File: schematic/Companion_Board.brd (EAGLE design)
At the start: 97 x 52 mm, 51 parts, among them J10 QSH-030-01-X-D-A, Q1 16MHz

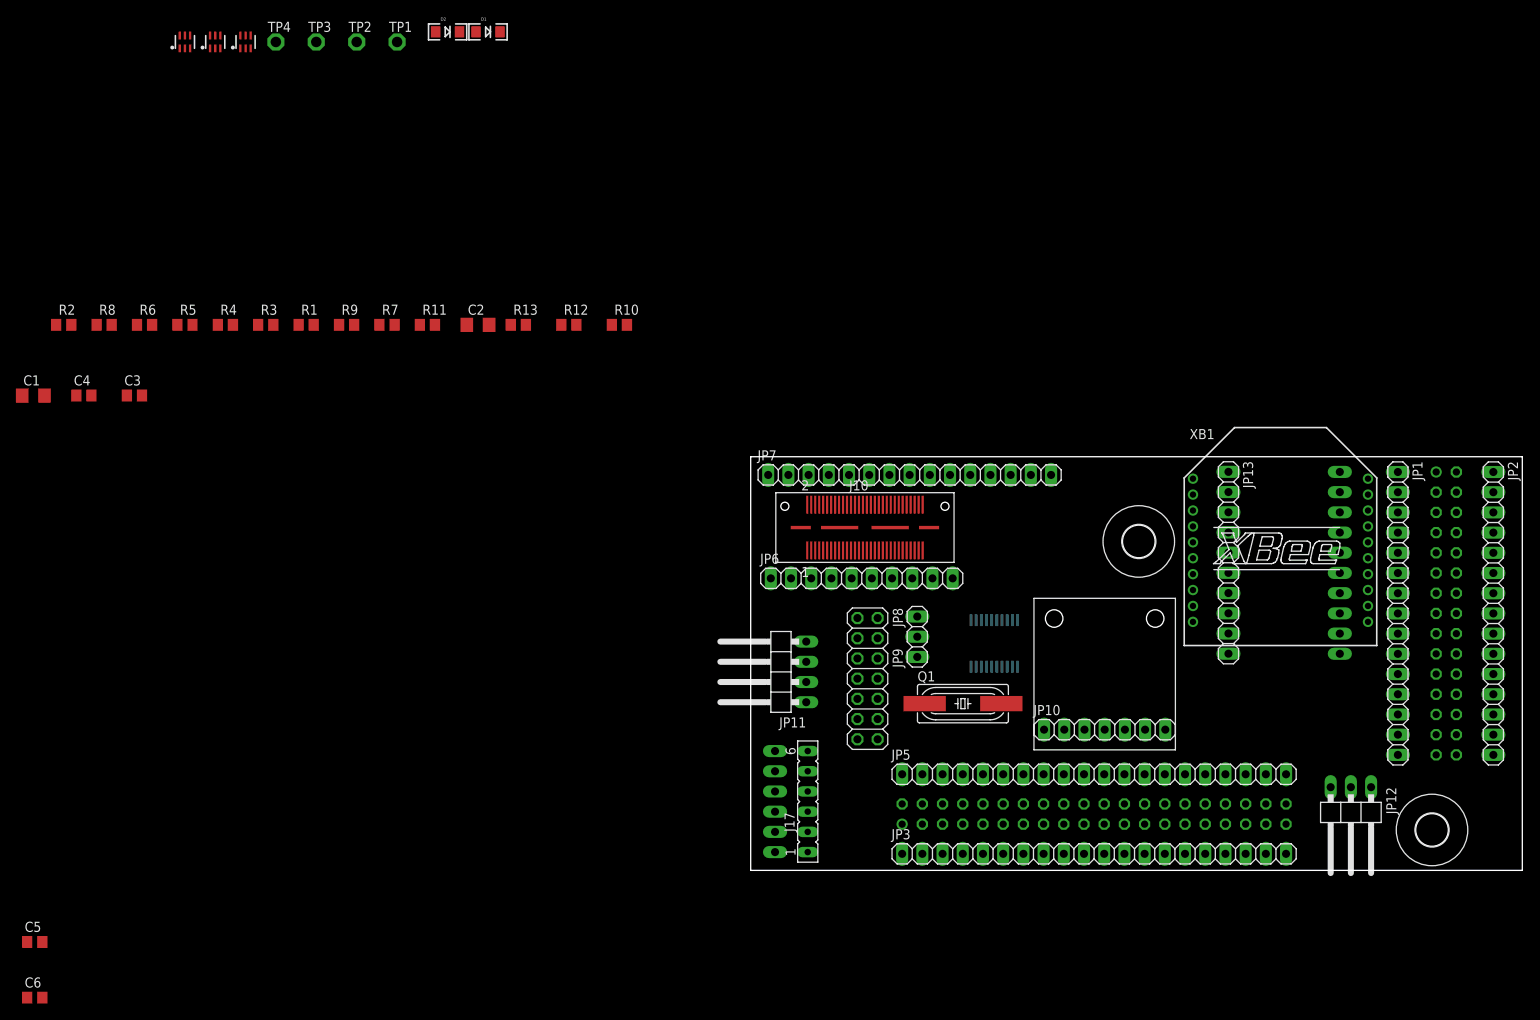
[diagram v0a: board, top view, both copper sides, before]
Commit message: Removed debug connector, now have parts laid out.
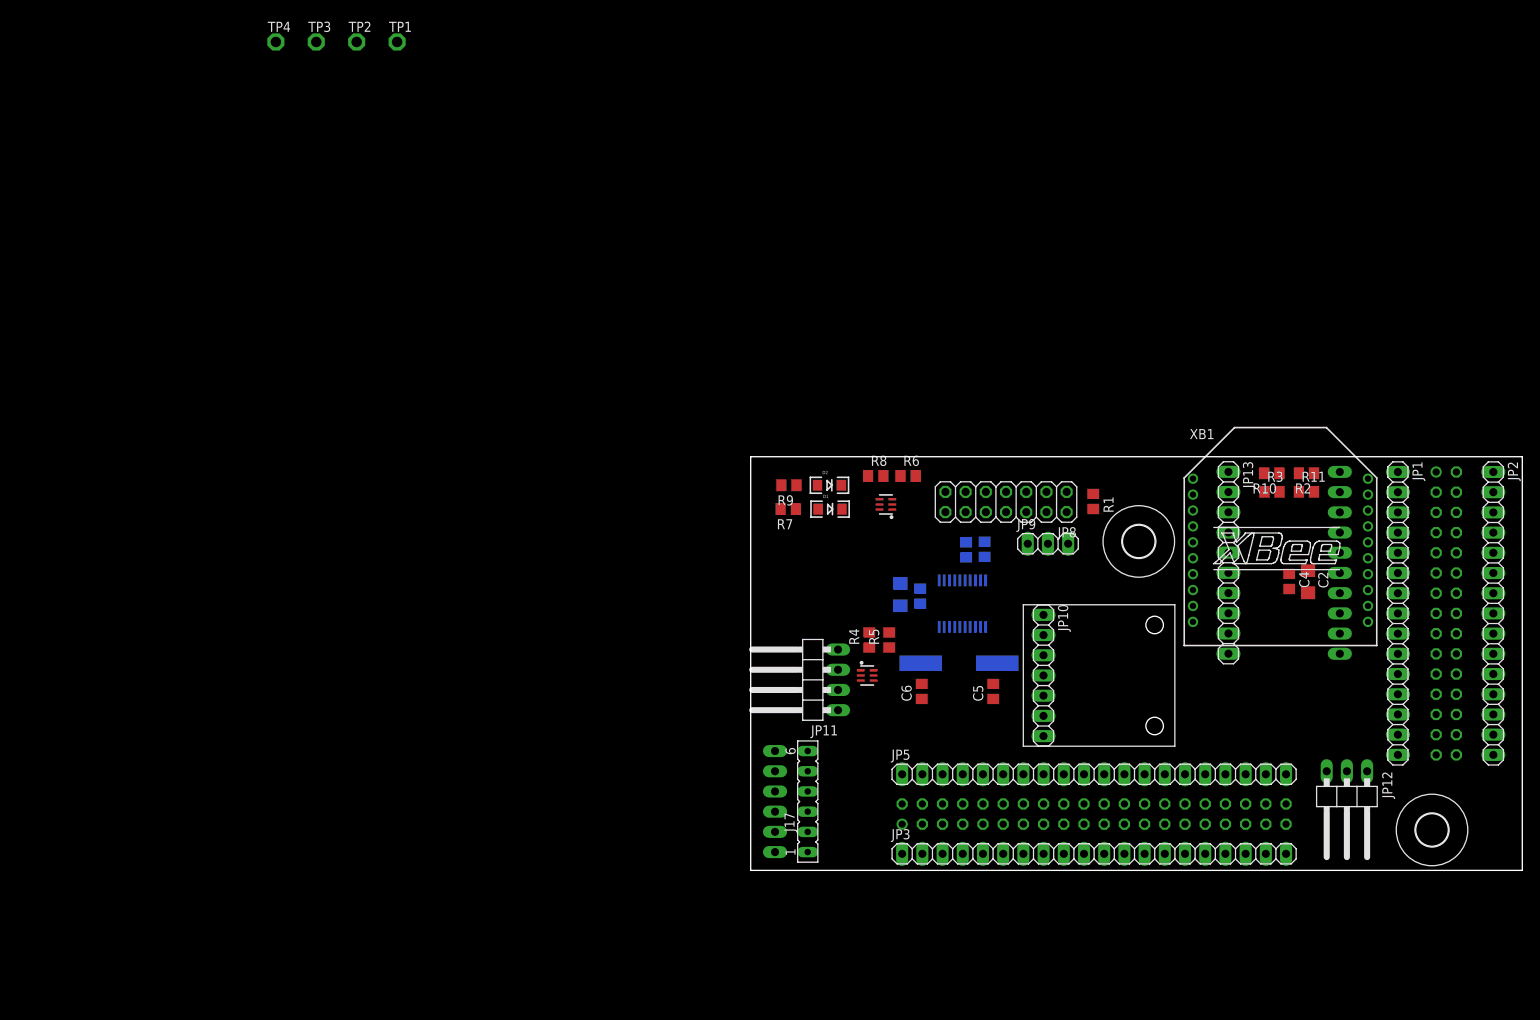
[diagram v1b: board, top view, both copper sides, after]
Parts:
- removed J10: QSH-030-01-X-D-A, QSH-030-01-X-D-A:QSH-030-01-X-D-A
- removed JP6: (no value), pinhead:1X10
- removed JP7: (no value), pinhead:1X15
- removed U$4: 2N7002DW, companion_board:SOT363
- moved R2 157.3 mm to (69.9, 49.9), turned to 180 degrees
- moved C4 153.3 mm to (67.7, 36.3), turned to 270 degrees
- moved R3 128.2 mm to (65.5, 47.6)
- moved C5 124.5 mm to (30.5, 22.5), turned to 90 degrees
- moved C6 118.0 mm to (21.5, 22.5), turned to 90 degrees
- moved R11 112.5 mm to (69.9, 47.6)
- moved C1 111.8 mm to (18.8, 34.7), flipped to the bottom, turned to 270 degrees
- moved U$2 111.6 mm to (14.6, 24.5), turned to 270 degrees
- moved C2 109.3 mm to (70.1, 36.3), turned to 270 degrees
- moved U$3 102.4 mm to (17.0, 46.0), turned to 90 degrees
- moved C3 101.9 mm to (21.3, 34.5), flipped to the bottom, turned to 270 degrees
- moved R1 101.4 mm to (43.1, 46.4), turned to 270 degrees
- moved R8 98.8 mm to (15.7, 49.6)
- moved R6 97.9 mm to (19.8, 49.6)
- moved R5 97.0 mm to (17.4, 29.0), turned to 90 degrees
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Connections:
- removed net ACOK: J10.1, JP6.3
- removed net D_FORCE_OFF_L: J10.55, JP6.8
- removed net FORCE_RECOVERY_R_L: J10.42, JP7.10
- removed net I2C_GP0_CLK_1V8: J10.16, JP7.7
- removed net I2C_GP0_DAT_1V8: J10.18, JP7.8
- removed net I2C_GP1_CLK_3V3_J10: J10.54, JP7.13
- removed net I2C_GP1_DAT_3V3_J10: J10.56, JP7.14
- removed net I2C_PM_CLK: J10.25, JP6.5
- removed net I2C_PM_DAT: J10.23, JP6.4
- removed net N$48 (its old number): J10.40, JP7.9
- removed net N$72: D2.C, U$4.6
- removed net UART1_CTS: J10.10, JP7.5
- removed net UART1_RXD_DBG_1V8: J10.8, JP7.4
- removed net UART1_TXD_DBG_1V8: J10.6, JP7.3
- removed net UART2_RXD_DBG: J10.29, JP6.7
- removed net UART2_TXD_DBG: J10.27, JP6.6
- removed net UAT1_RTS: J10.12, JP7.6
- removed net VDD_1V8: J10.21, JP6.1
- removed net VDD_1V8_J10: J10.2, JP7.1
- new net N$58: D2.C, U$3.3
- net +3V3: now also R3.1; no longer R3.2
- net DISABLE_DEADMAN: now also R2.2; no longer R2.1
- net FORCE_RESET: now also R3.2; no longer R3.1
- net GND: now also U$3.4; no longer J10.13, J10.14, J10.19, J10.24, J10.3, J10.35, J10.36, J10.4, J10.51, J10.52, J10.58, J10.61, J10.62, J10.63, J10.64, JP6.10, JP6.2, JP6.9, JP7.15, JP7.2, U$4.1
- net MSP_LED1: now also U$3.5; no longer U$4.2
- net POWER_BTN_R: no longer J10.46, JP7.12
- net RESET_IN_R_L: no longer J10.44, JP7.11
- net XBEE_DIO0: now also R2.1; no longer R2.2

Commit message: One iteration on board layout.
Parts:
- moved TP3 114.5 mm to (32.4, 29.6)
- moved TP2 112.1 mm to (31.5, 26.6)
- moved TP4 89.8 mm to (2.81, 39.6)
- moved TP1 82.8 mm to (2.75, 36.1)
- moved R5 10.7 mm to (15.1, 18.5), turned to 270 degrees
- moved R8 7.43 mm to (18.2, 42.6)
- moved Q1 4.50 mm to (26.2, 21.5)
- moved C5 4.00 mm to (30.5, 18.5)
- moved C6 4.00 mm to (21.5, 18.5)
- moved R10 2.00 mm to (65.5, 47.9)
- moved R11 2.00 mm to (69.9, 45.6)
- moved R2 2.00 mm to (69.9, 47.9)
- moved R3 2.00 mm to (65.5, 45.6)
- moved C1 1.80 mm to (17.3, 33.7)
- moved U$2 1.68 mm to (15.0, 22.9), turned to 180 degrees
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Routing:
- net +3V3: track 0.00 -> 221.5 mm, vias 0 -> 2
- net DISABLE_DEADMAN: track 0.00 -> 75.0 mm, vias 0 -> 1
- net FORCE_RESET: track 0.00 -> 69.5 mm, vias 0 -> 1
- net LIGHT_PWM1: track 0.00 -> 66.9 mm, vias 0 -> 1
- net LIGHT_PWM2: track 0.00 -> 60.7 mm, vias 0 -> 1
- net I2C_GP0_CLK_3V3: track 0.00 -> 57.6 mm, vias 0 -> 1
- net I2C_GP0_DAT_3V3: track 0.00 -> 50.7 mm, vias 0 -> 1
- net SBW_TDIO: track 0.00 -> 47.0 mm
- net SBW_TEST: track 0.00 -> 32.3 mm
- net N$57: track 0.00 -> 31.8 mm, vias 0 -> 1
- net GND: track 0.00 -> 28.6 mm, vias 0 -> 4
- net MSP_LED2: track 0.00 -> 28.4 mm, vias 0 -> 1
- net MSP_LED1: track 0.00 -> 24.0 mm, vias 0 -> 1
- net N$56: track 0.00 -> 24.0 mm, vias 0 -> 1
- net N$41: track 0.00 -> 17.1 mm, vias 0 -> 1
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- added copper zone on layer 1, net GND
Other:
- board text added: "3V3"
- board text added: "GND"

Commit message: First draft of board layout.
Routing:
- net N$35: track 0.00 -> 3.23 mm
- net I2C_GP0_DAT_3V3: track 50.7 -> 51.4 mm
- net LIGHT_PWM2: track 60.7 -> 61.3 mm

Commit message: Some corrections to layout.
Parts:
- renumbered TP2 to I2C_DAT, TP3 to I2C_CLK

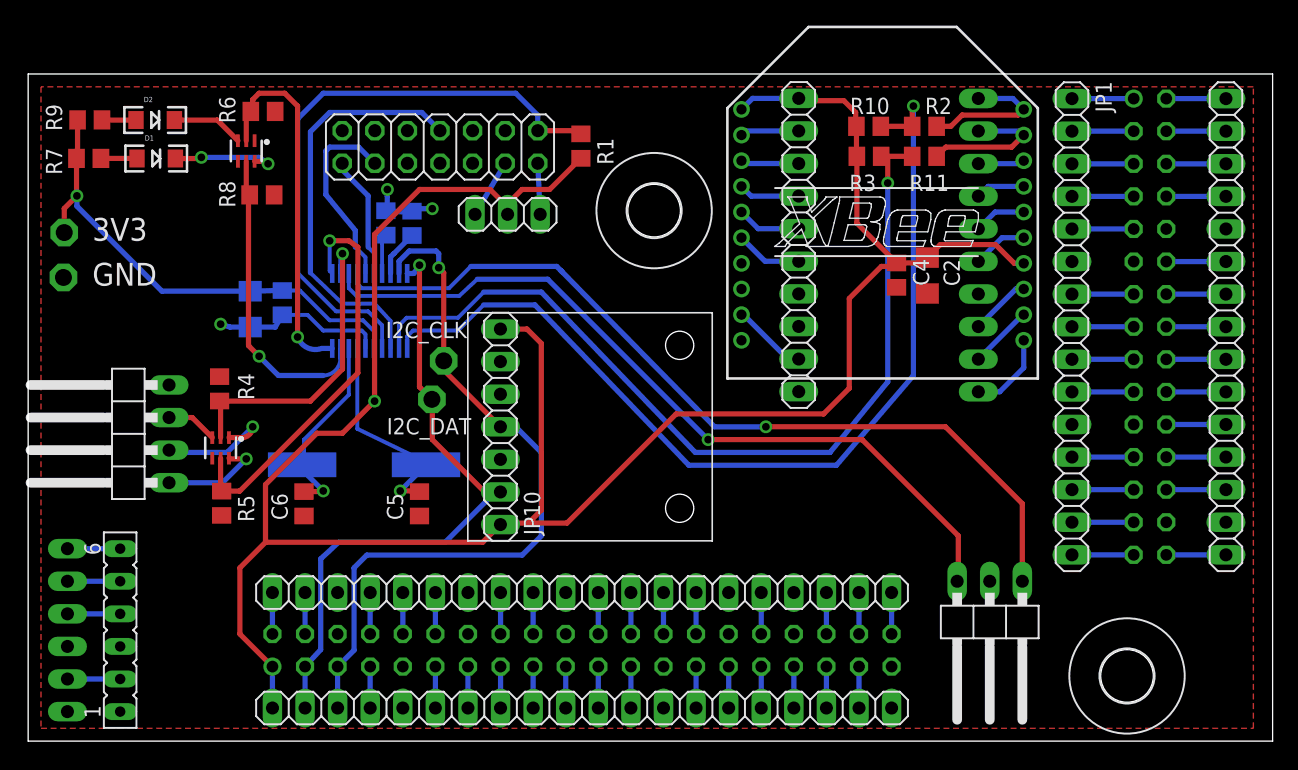
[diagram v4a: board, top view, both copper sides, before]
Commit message: Pre-production iteration on companion board, including BOM.
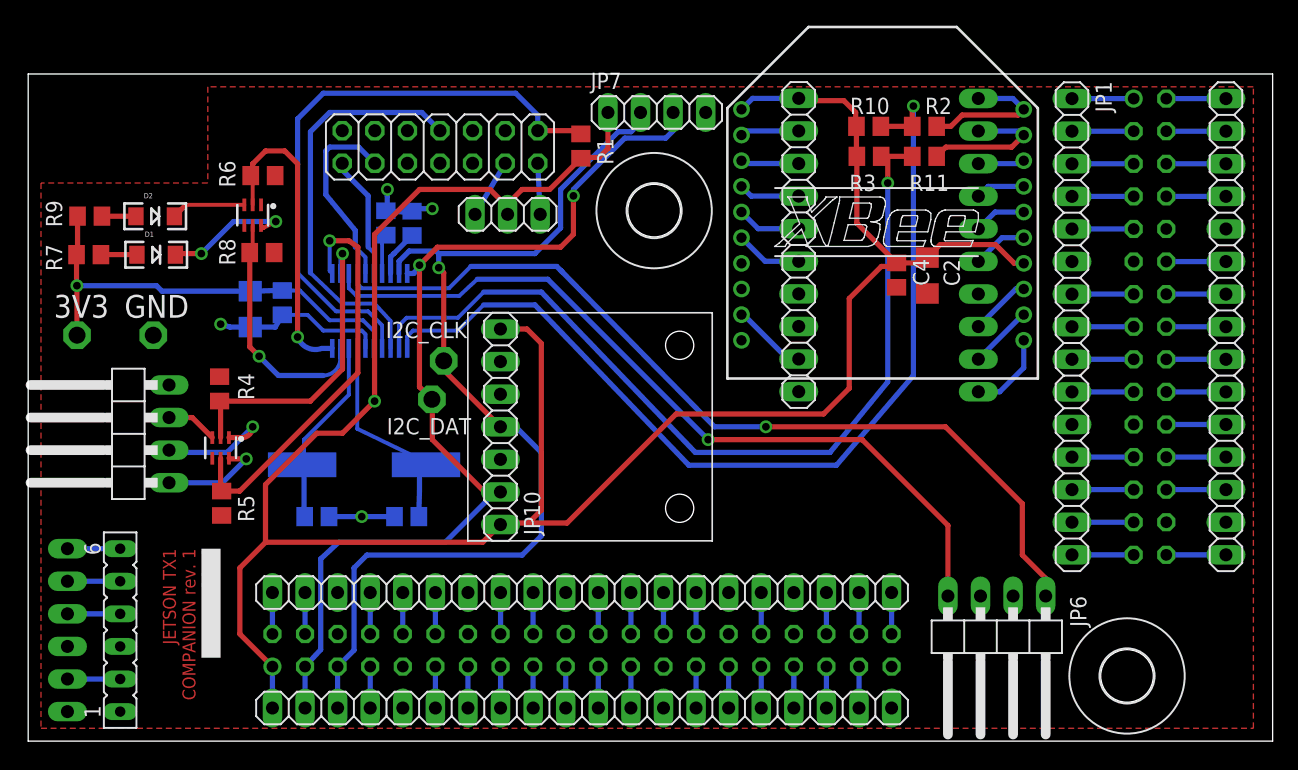
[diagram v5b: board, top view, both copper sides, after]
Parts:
- removed JP12: PWM Light Control, pinhead:1X03/90
- added JP6: (no value), pinhead:1X04/90
- added JP7: (no value), pinhead:1X04
- moved TP1 8.32 mm to (9.75, 31.6)
- moved TP4 8.06 mm to (3.81, 31.6)
- moved D1 7.50 mm to (9.98, 37.9)
- moved D2 7.50 mm to (9.90, 40.9)
- moved R7 7.50 mm to (4.72, 37.9)
- moved R9 7.50 mm to (4.80, 40.9)
- moved U$3 5.02 mm to (17.5, 41.0)
- moved R6 5.00 mm to (18.3, 44.1)
- moved R8 4.50 mm to (18.2, 38.1)
- moved C5 1.41 mm to (29.5, 17.5), flipped to the bottom, turned to 180 degrees
- moved C6 1.41 mm to (22.5, 17.5), flipped to the bottom, turned to 0 degrees
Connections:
- net +3V3: now also JP7.1
- net GND: now also JP6.2, JP6.3, JP7.4; no longer JP12.2
- net I2C_GP0_CLK_3V3: now also JP7.2
- net I2C_GP0_DAT_3V3: now also JP7.3
- net LIGHT_PWM1: now also JP6.1; no longer JP12.1
- net LIGHT_PWM2: now also JP6.4; no longer JP12.3
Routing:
- net I2C_GP0_DAT_3V3: track 51.4 -> 79.0 mm, vias 1 -> 2
- net I2C_GP0_CLK_3V3: track 57.6 -> 80.1 mm
- net MSP_LED1: track 24.0 -> 18.9 mm
- net GND: track 28.8 -> 33.9 mm, vias 4 -> 5
- net MSP_LED2: track 28.4 -> 24.1 mm
- net +3V3: track 221.5 -> 223.5 mm
- net LIGHT_PWM1: track 67.4 -> 69.3 mm
- net N$48: track 8.51 -> 10.2 mm
- net LIGHT_PWM2: track 61.3 -> 62.1 mm
- net N$41: track 17.1 -> 16.9 mm, vias 1 -> 0
- net N$47: track 14.9 -> 14.7 mm, vias 1 -> 0
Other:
- board text added: "JETSON TX1 COMPANION rev. 1 2016"
